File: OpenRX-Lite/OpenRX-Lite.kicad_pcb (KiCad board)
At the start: 6 copper layers, 10 x 10.5 mm, 47 parts, among them U1 ESP32-C3, U2 TLV75533PDQNR, U3 SX1281IMLTRT, X1 CJ17-400001010B20

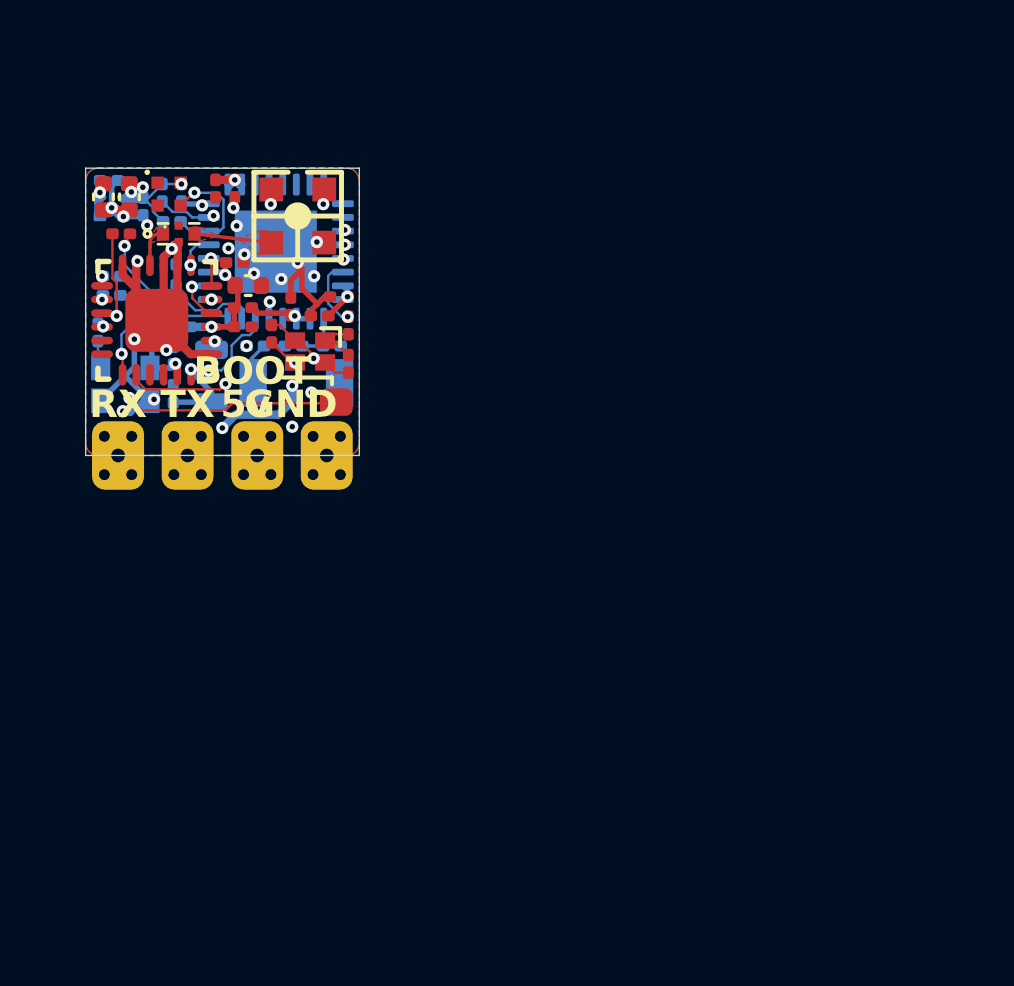
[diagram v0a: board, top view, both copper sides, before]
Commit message: feat(OpenRX-Lite): convert to AntAIO antweight battlebot AIO
Extend OpenRX-Lite (ESP32-C3 + SX1281 ELRS RX) into an integrated
1–2S antweight combat-robot controller in the Malenki-Nano style:

- Triple brushed-DC ESC: 3× DRV8212 (U6/U10 drive, U11 weapon)
- 6-axis IMU LSM6DS3TR-C (U2) on the shared radio SPI bus
- Power: TPS63070 buck-boost (+BATT→5V) + TLV75533 LDO (→3V3),
  AON7407 reverse-polarity P-FET
- New footprints/3D: DFN-8, WSON-8, VQFN-15, LGA-14, SOD-923, IND 2.0×1.6
- Add part datasheets (DRV8212, LSM6DS3TR-C, TPS63070, AON7407)
- CHANGELIST.md: verified open/done items
- REVIEW.md: multi-agent pin/datasheet/electrical design review

Co-Authored-By: Claude Opus 4.8 (1M context) <noreply@anthropic.com>
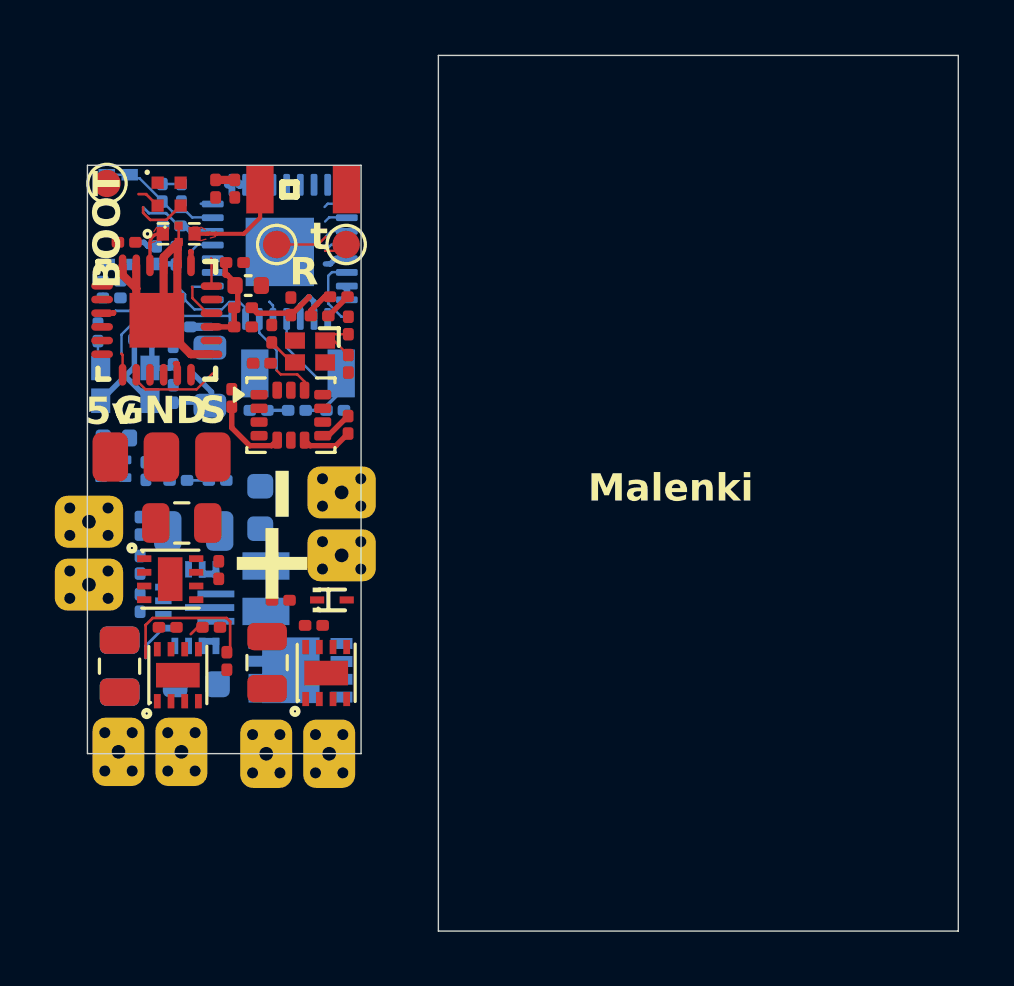
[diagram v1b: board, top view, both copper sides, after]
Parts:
- removed C10: 1uF, Capacitor_SMD:C_0201_0603Metric
- removed C16, C8: 10uF, Capacitor_SMD:C_0402_1005Metric
- removed R2: 10k, Resistor_SMD:R_0201_0603Metric
- removed TP4: GND, OpenRX-Shared:SolderPad_1.2x2.0mm
- removed TP5: BOOT, OpenRX-Shared:SolderPad_1.2x2.0mm
- added C18: 100nF, Capacitor_SMD:C_0201_0603Metric, F.Cu at (105.3, 107.9)
- added C29: 100nF, Capacitor_SMD:C_0201_0603Metric, F.Cu at (108.3, 116.2)
- added C30: 100nF, Capacitor_SMD:C_0201_0603Metric, F.Cu at (103.0, 116.3)
- added C32: 22uF, Capacitor_SMD:C_0805_2012Metric, F.Cu at (106.6, 117.6)
- added C33: 22uF, Capacitor_SMD:C_0805_2012Metric, F.Cu at (101.2, 117.7)
- added C34: 22uF, Capacitor_SMD:C_0805_2012Metric, B.Cu at (101.2, 117.7)
- added C35: 10uF, Capacitor_SMD:C_0603_1608Metric, B.Cu at (104.0, 118.4)
- added C36: 100nF, Capacitor_SMD:C_0201_0603Metric, B.Cu at (102.0, 115.4)
- added C37: 10uF, Capacitor_SMD:C_0603_1608Metric, B.Cu at (106.4, 111.9)
- added C38: 22uF, Capacitor_SMD:C_0805_2012Metric, B.Cu at (104.0, 112.8)
- added C40: 1uF, Capacitor_SMD:C_0201_0603Metric, B.Cu at (102.2, 110.6)
- added C41: 10uF, Capacitor_SMD:C_0402_1005Metric, B.Cu at (101.1, 109.4)
- added C42: 22uF, Capacitor_SMD:C_0805_2012Metric, F.Cu at (103.5, 112.5)
- added C43: 100nF, Capacitor_SMD:C_0201_0603Metric, F.Cu at (104.9, 114.2)
- added L6: FTC201612S1R5MBCA, OpenRX-Shared:IND-SMD_L2.0-W1.6, B.Cu at (106.6, 114.9)
- added Q2: AON7407, OpenRX-Shared:DFN-8_L3.0-W3.0-P0.65-BL, B.Cu at (107.8, 117.8)
- added R11: 52.3k, Resistor_SMD:R_0201_0603Metric, B.Cu at (104.8, 110.9)
- added R12: 10k, Resistor_SMD:R_0201_0603Metric, B.Cu at (103.4, 110.9)
- added R13: 10k, Resistor_SMD:R_0201_0603Metric, F.Cu at (107.1, 115.3)
- added R14: 100k, Resistor_SMD:R_0201_0603Metric, F.Cu at (105.2, 117.5)
- added R15: 100k, Resistor_SMD:R_0201_0603Metric, F.Cu at (104.6, 116.3)
- added R16: 52.3k, Resistor_SMD:R_0201_0603Metric, B.Cu at (102.0, 112.6)
- added R17: 10k, Resistor_SMD:R_0201_0603Metric, B.Cu at (102.0, 114.0)
- added R6: 10k, Resistor_SMD:R_0201_0603Metric, F.Cu at (101.5, 102.2)
- added R8: 10k, Resistor_SMD:R_0201_0603Metric, F.Cu at (106.4, 106.6)
- added TP10: M+, OpenRX-Shared:SolderPad_1.2x2.0mm, F.Cu at (103.5, 120.8)
- added TP11: M-, OpenRX-Shared:SolderPad_1.2x2.0mm, F.Cu at (101.2, 120.8)
- added TP12: M+, OpenRX-Shared:SolderPad_1.2x2.0mm, F.Cu at (100.1, 114.7)
- added TP13: M-, OpenRX-Shared:SolderPad_1.2x2.0mm, F.Cu at (100.1, 112.4)
- added TP14: gnd, OpenRX-Shared:SolderPad_1.2x2.0mm, F.Cu at (100.9, 110.1)
- added TP15: 5v, OpenRX-Shared:SolderPad_1.2x2.0mm, F.Cu at (102.8, 110.1)
- added TP16: S, OpenRX-Shared:SolderPad_1.2x2.0mm, F.Cu at (104.7, 110.1)
- added TP6: B+, OpenRX-Shared:SolderPad_1.2x2.0mm, F.Cu at (109.4, 113.7)
- added TP7: B+, OpenRX-Shared:SolderPad_1.2x2.0mm, F.Cu at (109.4, 111.3)
- added TP8: M+, OpenRX-Shared:SolderPad_1.2x2.0mm, F.Cu at (108.9, 120.9)
- added TP9: M-, OpenRX-Shared:SolderPad_1.2x2.0mm, F.Cu at (106.6, 120.9)
- added U10: DRV8212DSGR, OpenRX-Shared:WSON-8_L2.0-W2.0-P0.50-TL-EP, F.Cu at (103.4, 118.0)
- added U11: DRV8212DSGR, OpenRX-Shared:WSON-8_L2.0-W2.0-P0.50-TL-EP, F.Cu at (103.1, 114.5)
- added U4: TLV75533PDQNR, OpenRX-Shared:X2SON-4_L1.0-W1.0-P0.65-TL-EP, B.Cu at (101.0, 110.5)
- added U6: DRV8212DSGR, OpenRX-Shared:WSON-8_L2.0-W2.0-P0.50-TL-EP, F.Cu at (108.8, 118.0)
- added U7: NZ9F6V2ST5G, OpenRX-Shared:SOD-923_L0.8-W0.6-LS1.0-RD, F.Cu at (109.0, 115.3)
- added U8: TPS63070RNMR, OpenRX-Shared:VQFN-15_L3.0-W2.5-P0.50-BL, B.Cu at (103.8, 115.6)
- added U9: TS2306A 240GF MSM 9_C2976675, OpenRX-Shared:SW-SMD_4P-L3.0-W2.0-P0.85-LS3.5, B.Cu at (101.2, 101.4)
- AE2: value 47948-0001 -> 2450AT18A100E; footprint OpenRX-Shared:ANT-SMD_47948-0001 -> OpenRX-Shared:ANT-SMD_L3.2-W1.6
- C15: value 1uF -> 100nF; moved to F.Cu
- TP1: value RX -> TestPoint; footprint OpenRX-Shared:SolderPad_1.2x2.0mm -> TestPoint:TestPoint_Pad_D1.0mm
- TP2: value TX -> TestPoint; footprint OpenRX-Shared:SolderPad_1.2x2.0mm -> TestPoint:TestPoint_Pad_D1.0mm
- TP3: value 5V -> TestPoint; footprint OpenRX-Shared:SolderPad_1.2x2.0mm -> TestPoint:TestPoint_Pad_D1.0mm
- U2: value TLV75533PDQNR -> LSM6DS3TR-C; footprint OpenRX-Shared:X2SON-4_L1.0-W1.0-P0.65-TL-EP -> Package_LGA:LGA-14_3x2.5mm_P0.5mm_LayoutBorder3x4y; moved to F.Cu
- moved TP3 11.4 mm to (100.8, 100.1)
- moved TP1 11.4 mm to (109.5, 102.3), turned to 180 degrees
- moved C15 10.9 mm to (109.6, 108.9)
- moved U2 10.0 mm to (107.5, 108.5), turned to 0 degrees
- moved TP2 8.37 mm to (107.0, 102.3), turned to -170 degrees
- moved C21 3.75 mm to (109.1, 108.3), turned to 0 degrees
- moved C22 3.56 mm to (106.3, 108.3), turned to 180 degrees
- moved L2 2.35 mm to (107.7, 108.3), turned to 180 degrees
- moved R5 1.59 mm to (102.6, 102.7), turned to 90 degrees
- moved AE2 0.99 mm to (108.0, 100.3)
- moved AE1 0.36 mm to (107.8, 107.0), turned to 180 degrees
- moved C27 0.18 mm to (101.0, 103.6)
- moved R3 0.16 mm to (103.2, 101.6)
- moved U1 0.15 mm to (107.1, 102.6)
- moved C26 0.09 mm to (101.0, 104.2)
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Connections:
- AE2 pad 1: GND -> Net-(FL1-OUT)
- AE2 pad 2: GND -> unconnected-(AE2-Pad2)
- TP1 pad 1: Net-(U1-U0RXD) -> /ESP32-C3 + SX1281 Core (UFL)/RIGHT_EN
- TP2 pad 1: Net-(U1-U0TXD) -> /ESP32-C3 + SX1281 Core (UFL)/RIGHT_PH
- TP3 pad 1: +5V -> /ESP32-C3 + SX1281 Core (UFL)/BOOT
- U1 pad 16: GND -> /ESP32-C3 + SX1281 Core (UFL)/WEAPON_EN
- U1 pad 25: unconnected-(U1-GPIO18-Pad25) -> /ESP32-C3 + SX1281 Core (UFL)/LEFT_PH
- U1 pad 26: unconnected-(U1-GPIO19-Pad26) -> /ESP32-C3 + SX1281 Core (UFL)/LEFT_EN
- U1 pad 27: Net-(U1-U0RXD) -> /ESP32-C3 + SX1281 Core (UFL)/RIGHT_PH
- U1 pad 28: Net-(U1-U0TXD) -> /ESP32-C3 + SX1281 Core (UFL)/RIGHT_EN
- U1 pad 4: unconnected-(U1-XTAL_32K_P-Pad4) -> /ESP32-C3 + SX1281 Core (UFL)/VSENSE
- U1 pad 6: /ESP32-C3 + SX1281 Core (UFL)/RST -> /ESP32-C3 + SX1281 Core (UFL)/IMU_CS
- U2 pad 1: +3V3 -> /ESP32-C3 + SX1281 Core (UFL)/MISO
- U2 pad 3: +5V -> GND
- U2 pad 4: +5V -> unconnected-(U2-INT1-Pad4)
- U2 pad 5: GND -> +3V3
- U3 pad 3: /ESP32-C3 + SX1281 Core (UFL)/RST -> /ESP32-C3 + SX1281 Core (UFL)/CHIP_EN
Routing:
- net /ESP32-C3 + SX1281 Core (UFL)/BOOT: track 19.5 -> 4.64 mm, vias 2 -> 0
- net +5V: track 13.7 -> 0.00 mm, vias 1 -> 0
- net Net-(U1-U0RXD): track 12.4 -> 0.00 mm, vias 1 -> 0
- net /ESP32-C3 + SX1281 Core (UFL)/RST: track 10.9 -> 0.00 mm, vias 2 -> 0
- net Net-(U1-U0TXD): track 10.2 -> 0.00 mm, vias 1 -> 0
- net GND: track 30.2 -> 20.8 mm, vias 25 -> 0
- net Net-(U8-PS/SYNC): track 0.00 -> 6.98 mm
- net +3V3: track 22.4 -> 16.1 mm, vias 11 -> 0
- net /ESP32-C3 + SX1281 Core (UFL)/CHIP_EN: track 4.21 -> 8.35 mm
- net /ESP32-C3 + SX1281 Core (UFL)/IMU_CS: track 0.00 -> 3.65 mm
- net /ESP32-C3 + SX1281 Core (UFL)/VSENSE: track 0.00 -> 3.46 mm
- net /ESP32-C3 + SX1281 Core (UFL)/NSS: track 1.53 -> 4.58 mm, vias 1 -> 0
- net /ESP32-C3 + SX1281 Core (UFL)/RIGHT_PH: track 0.00 -> 2.66 mm
- net Net-(C25-Pad1): track 2.30 -> 4.31 mm, vias 1 -> 0
- net /ESP32-C3 + SX1281 Core (UFL)/RIGHT_EN: track 0.00 -> 1.68 mm
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- removed copper zone on In2.Cu, net +3V3
- removed copper zone on B.Cu, net GND
- removed copper zone on In1.Cu, net GND
- removed copper zone on In3.Cu, net GND
- removed copper zone on In4.Cu, net GND
- removed copper zone on F.Cu, net Net-(FL1-OUT)
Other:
- board size 10 x 10.5 mm -> 31.8 x 32 mm
- board text added: "+"
- board text added: "-"
- board text added: "ANT-AIO V1"
- board text added: "Malenki"
- board text added: "R"
- board text added: "S"
- board text added: "t"
- board text removed: "RX"
- board text removed: "TX"
- board text removed: "open"
